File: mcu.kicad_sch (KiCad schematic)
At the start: 23 parts, among them J10 Conn_01x16, J8 Conn_01x12, U3 W25Q64JVSSIQ, U9 MDBT50Q-1MV2, Y1 ABS06-32.768KHZ-1-T

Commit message: Release candidate
Changed USBC connector, changed TagConnect to use footprint with legs, move NRF52 to edge of board, clean up traces
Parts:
- D4, D5: MP LTST-S270TBKT -> LTST-C191TBKT
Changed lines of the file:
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@@
 			)
 		)
-		(property "Datasheet" "https://optoelectronics.liteon.com/upload/download/DS22-2000-175/LTST-S270TBKT.pdf"
+		(property "Datasheet" "https://optoelectronics.liteon.com/upload/download/DS22-2000-230/LTST-C191TBKT.pdf"
 			(at 77.47 184.15 0)
 			(effects
@@
 			)
 		)
-		(property "MP" "LTST-S270TBKT"
+		(property "MP" "LTST-C191TBKT"
 			(at 77.47 184.15 0)
 			(effects
@@
 			)
 		)
-		(property "Datasheet" "https://optoelectronics.liteon.com/upload/download/DS22-2000-175/LTST-S270TBKT.pdf"
+		(property "Datasheet" "https://optoelectronics.liteon.com/upload/download/DS22-2000-230/LTST-C191TBKT.pdf"
 			(at 43.18 184.15 0)
 			(effects
@@
 			)
 		)
-		(property "MP" "LTST-S270TBKT"
+		(property "MP" "LTST-C191TBKT"
 			(at 43.18 184.15 0)
 			(effects

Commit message: Update part numbers
Update part numbers for 12 and 16 PIN SMD 2.54mm pins and USB-C 2.0 connector.
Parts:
- J10: MP M20-8771642R -> TSM-116-01-T-SV-P-TR
- J8: MP M20-8771246 -> 1-1241150-2
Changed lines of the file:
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@@
 			)
 		)
-		(property "Datasheet" "https://www.we-online.com/components/products/datasheet/61301211121.pdf"
+		(property "Datasheet" "https://www.te.com/usa-en/product-1-1241150-2.datasheet.pdf"
 			(at 234.95 55.88 0)
 			(effects
@@
 			)
 		)
-		(property "MP" "M20-8771246"
+		(property "MP" "1-1241150-2"
 			(at 234.95 55.88 0)
 			(effects
@@
 			)
 		)
-		(property "Datasheet" "https://www.we-online.com/components/products/datasheet/61301611121.pdf"
+		(property "Datasheet" "https://suddendocs.samtec.com/catalog_english/tsm.pdf"
 			(at 266.7 50.8 0)
 			(effects
@@
 			)
 		)
-		(property "MP" "M20-8771642R"
-			(at 266.7 50.8 0)
-			(effects
+		(property "MP" "TSM-116-01-T-SV-P-TR"
+			(at 266.7 50.8 0)
+			(effects

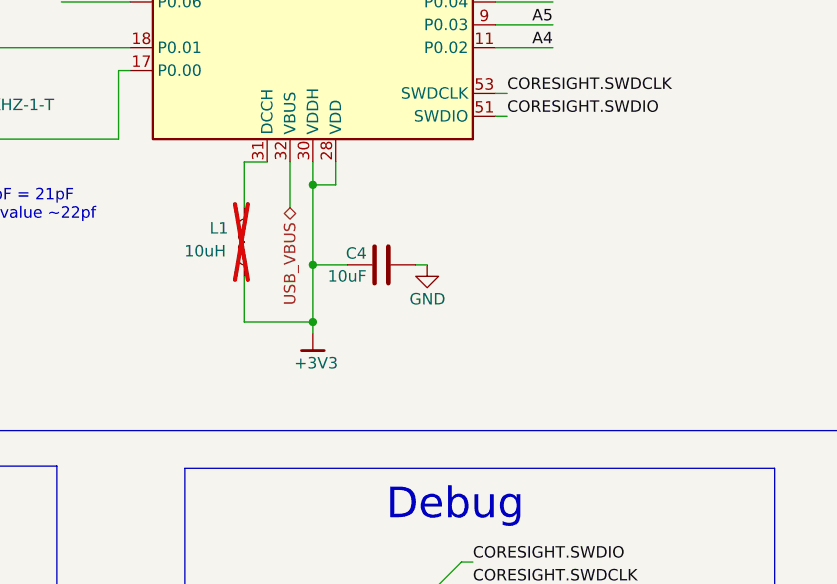
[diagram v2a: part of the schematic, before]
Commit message: Add bypass capacitor
Added bypass capacitor on VBUS for MCU
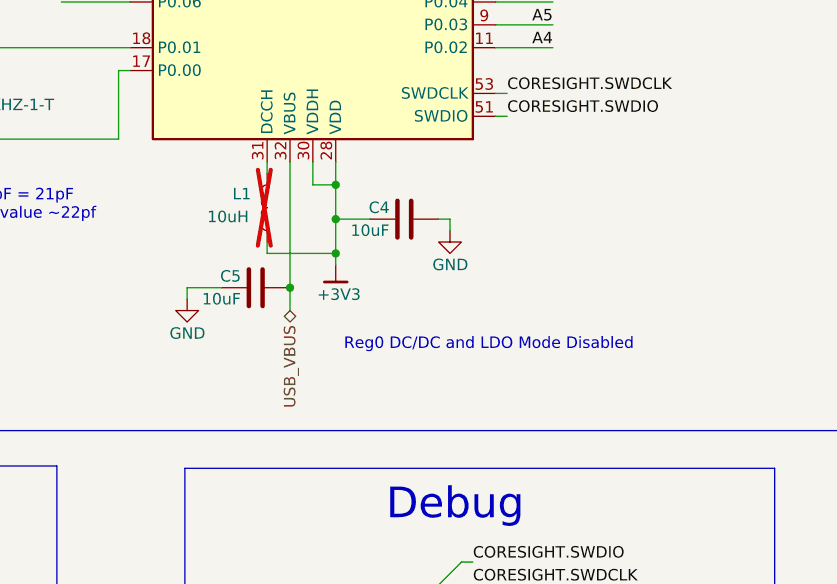
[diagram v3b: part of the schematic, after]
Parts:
- added C5: 10uF, Capacitor_SMD:C_0603_1608Metric, symbol Device:C
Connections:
- net GND: now also C5.2
- net USB_VBUS: now also C5.1
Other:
- note added: "Reg0 DC/DC and LDO Mode Disabled"
- moved on the sheet: C4, L1
